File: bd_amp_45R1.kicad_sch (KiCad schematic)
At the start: 53 parts, among them Q2101 2SC3357, Q2102 2SC3357, T2101 XFMR_RF_BIFILAR, T2102 XFMR_RF_BIFILAR, U2101 AS169-73, U2102 AS169-73

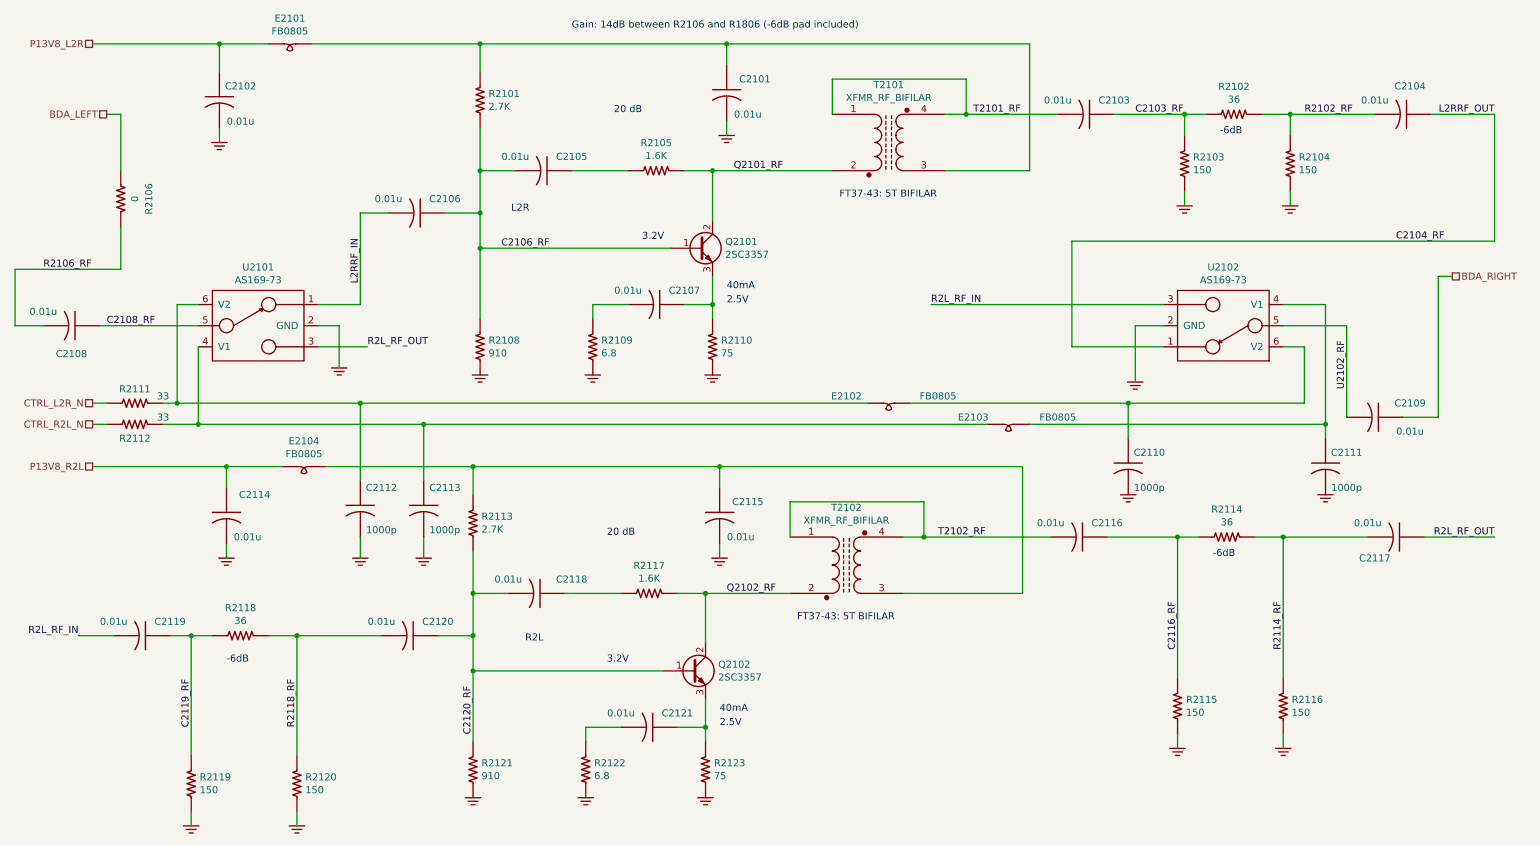
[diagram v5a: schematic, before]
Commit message: trx_mobo_concept_2_B. Change design to use a dedicated 8V supply for the 2SC3357 parts. Add S-Meter connector. Change mic connector to 3 pins and add 8V sopower supply to pin 3.
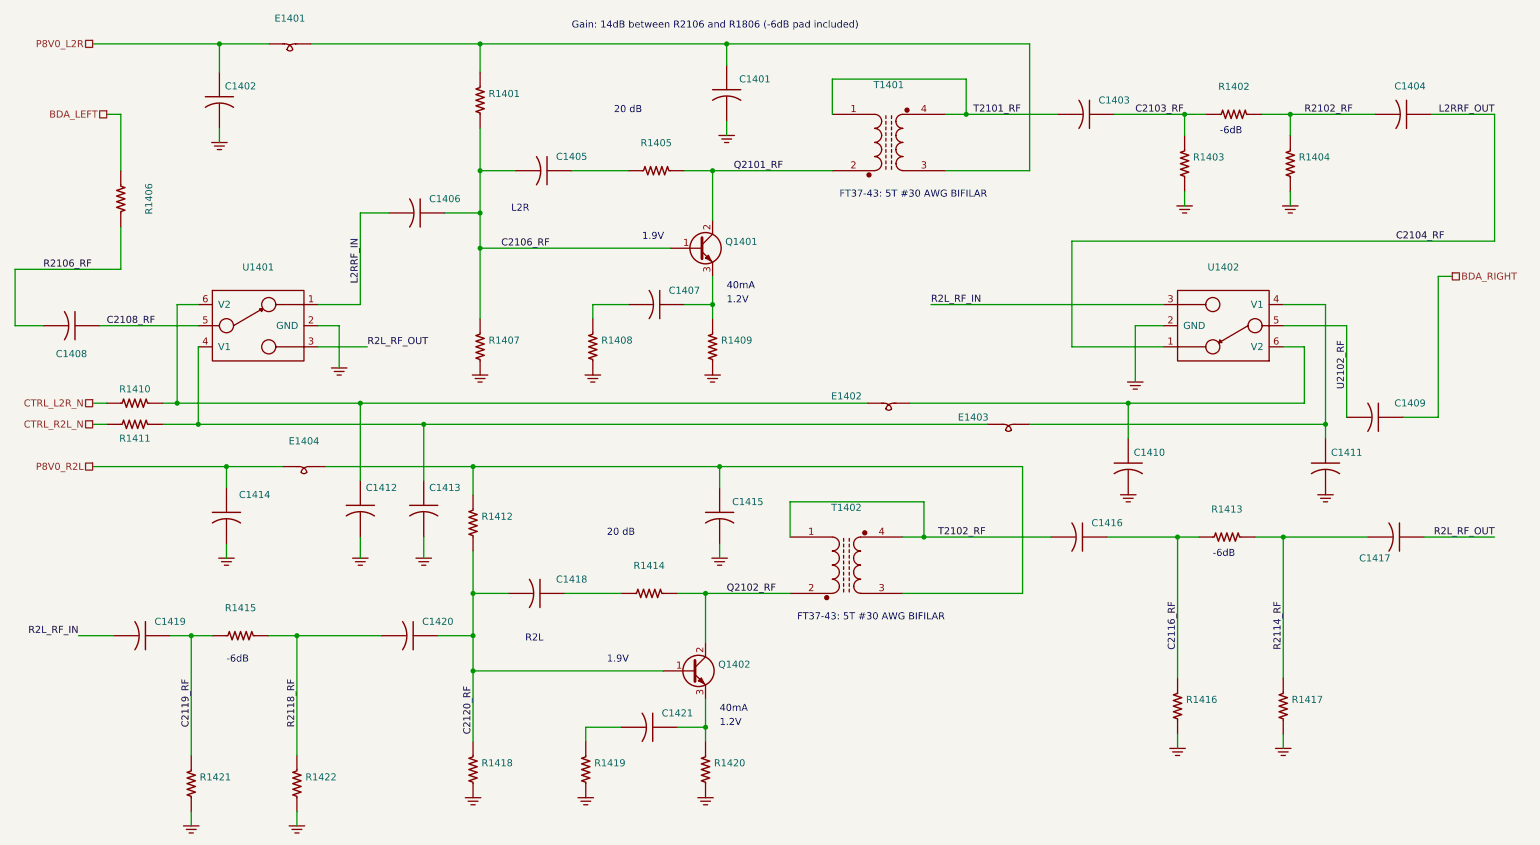
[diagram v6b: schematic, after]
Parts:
- C1401: renamed from C2101; value 0.01u -> (none); footprint Capacitor_SMD:C_0805_2012Metric_Pad1.18x1.45mm_HandSolder -> (none); PartNumber 800238-103 -> 800239-103
- C1402: renamed from C2102; value 0.01u -> (none); footprint Capacitor_SMD:C_0805_2012Metric_Pad1.18x1.45mm_HandSolder -> (none); PartNumber 800238-103 -> 800239-103
- C1403: renamed from C2103; value 0.01u -> (none); footprint Capacitor_SMD:C_0805_2012Metric_Pad1.18x1.45mm_HandSolder -> (none); PartNumber 800238-103 -> 800239-103
- C1404: renamed from C2104; value 0.01u -> (none); footprint Capacitor_SMD:C_0805_2012Metric_Pad1.18x1.45mm_HandSolder -> (none); PartNumber 800238-103 -> 800239-103
- C1405: renamed from C2105; value 0.01u -> (none); footprint Capacitor_SMD:C_0805_2012Metric_Pad1.18x1.45mm_HandSolder -> (none); PartNumber 800238-103 -> 800239-103
- C1406: renamed from C2106; value 0.01u -> (none); footprint Capacitor_SMD:C_0805_2012Metric_Pad1.18x1.45mm_HandSolder -> (none); PartNumber 800238-103 -> 800239-103
- C1407: renamed from C2107; value 0.01u -> (none); footprint Capacitor_SMD:C_0805_2012Metric_Pad1.18x1.45mm_HandSolder -> (none); PartNumber 800238-103 -> 800239-103
- C1408: renamed from C2108; value 0.01u -> (none); footprint Capacitor_SMD:C_0805_2012Metric_Pad1.18x1.45mm_HandSolder -> (none); PartNumber 800238-103 -> 800239-103
- C1409: renamed from C2109; value 0.01u -> (none); footprint Capacitor_SMD:C_0805_2012Metric_Pad1.18x1.45mm_HandSolder -> (none); PartNumber 800238-103 -> 800239-103
- C1410: renamed from C2110; value 1000p -> (none); footprint Capacitor_SMD:C_0805_2012Metric_Pad1.18x1.45mm_HandSolder -> (none)
- C1411: renamed from C2111; value 1000p -> (none); footprint Capacitor_SMD:C_0805_2012Metric_Pad1.18x1.45mm_HandSolder -> (none)
- C1412: renamed from C2112; value 1000p -> (none); footprint Capacitor_SMD:C_0805_2012Metric_Pad1.18x1.45mm_HandSolder -> (none)
- C1413: renamed from C2113; value 1000p -> (none); footprint Capacitor_SMD:C_0805_2012Metric_Pad1.18x1.45mm_HandSolder -> (none)
- C1414: renamed from C2114; value 0.01u -> (none); footprint Capacitor_SMD:C_0805_2012Metric_Pad1.18x1.45mm_HandSolder -> (none); PartNumber 800238-103 -> 800239-103
- C1415: renamed from C2115; value 0.01u -> (none); footprint Capacitor_SMD:C_0805_2012Metric_Pad1.18x1.45mm_HandSolder -> (none); PartNumber 800238-103 -> 800239-103
- C1416: renamed from C2116; value 0.01u -> (none); footprint Capacitor_SMD:C_0805_2012Metric_Pad1.18x1.45mm_HandSolder -> (none); PartNumber 800238-103 -> 800239-103
- C1417: renamed from C2117; value 0.01u -> (none); footprint Capacitor_SMD:C_0805_2012Metric_Pad1.18x1.45mm_HandSolder -> (none); PartNumber 800238-103 -> 800239-103
- C1418: renamed from C2118; value 0.01u -> (none); footprint Capacitor_SMD:C_0805_2012Metric_Pad1.18x1.45mm_HandSolder -> (none); PartNumber 800238-103 -> 800239-103
- C1419: renamed from C2119; value 0.01u -> (none); footprint Capacitor_SMD:C_0805_2012Metric_Pad1.18x1.45mm_HandSolder -> (none); PartNumber 800238-103 -> 800239-103
- C1420: renamed from C2120; value 0.01u -> (none); footprint Capacitor_SMD:C_0805_2012Metric_Pad1.18x1.45mm_HandSolder -> (none); PartNumber 800238-103 -> 800239-103
- C1421: renamed from C2121; value 0.01u -> (none); footprint Capacitor_SMD:C_0805_2012Metric_Pad1.18x1.45mm_HandSolder -> (none); PartNumber 800238-103 -> 800239-103
- E1401: renamed from E2101; value FB0805 -> (none); footprint Inductor_SMD:L_0805_2012Metric -> (none)
- E1402: renamed from E2102; value FB0805 -> (none); footprint Inductor_SMD:L_0805_2012Metric -> (none)
- E1403: renamed from E2103; value FB0805 -> (none); footprint Inductor_SMD:L_0805_2012Metric -> (none)
- E1404: renamed from E2104; value FB0805 -> (none); footprint Inductor_SMD:L_0805_2012Metric -> (none)
- Q1401: renamed from Q2101; value 2SC3357 -> (none); footprint Package_TO_SOT_SMD:SOT-89-3 -> (none)
- Q1402: renamed from Q2102; value 2SC3357 -> (none); footprint Package_TO_SOT_SMD:SOT-89-3 -> (none)
- R1401: renamed from R2101; value 2.7K -> (none); footprint Resistor_SMD:R_0805_2012Metric_Pad1.15x1.40mm_HandSolder -> (none); PartNumber 800235-272 -> 800235-112
- R1402: renamed from R2102; value 36 -> (none); footprint Resistor_SMD:R_0805_2012Metric_Pad1.15x1.40mm_HandSolder -> (none)
- R1403: renamed from R2103; value 150 -> (none); footprint Resistor_SMD:R_0805_2012Metric_Pad1.15x1.40mm_HandSolder -> (none)
- R1404: renamed from R2104; value 150 -> (none); footprint Resistor_SMD:R_0805_2012Metric_Pad1.15x1.40mm_HandSolder -> (none)
- R1405: renamed from R2105; value 1.6K -> (none); footprint Resistor_SMD:R_0805_2012Metric_Pad1.15x1.40mm_HandSolder -> (none)
- R1406: renamed from R2106; value 0 -> (none); footprint Resistor_SMD:R_0805_2012Metric_Pad1.15x1.40mm_HandSolder -> (none)
- R1407: renamed from R2108; value 910 -> (none); footprint Resistor_SMD:R_0805_2012Metric_Pad1.15x1.40mm_HandSolder -> (none); PartNumber 800235-911 -> 800235-361
- R1408: renamed from R2109; value 6.8 -> (none); footprint Resistor_SMD:R_0805_2012Metric_Pad1.15x1.40mm_HandSolder -> (none)
- R1409: renamed from R2110; value 75 -> (none); footprint Resistor_SMD:R_0805_2012Metric_Pad1.15x1.40mm_HandSolder -> (none); PartNumber 800235-750 -> 800235-300
- R1410: renamed from R2111; value 33 -> (none); footprint Resistor_SMD:R_0805_2012Metric_Pad1.15x1.40mm_HandSolder -> (none)
- R1411: renamed from R2112; value 33 -> (none); footprint Resistor_SMD:R_0805_2012Metric_Pad1.15x1.40mm_HandSolder -> (none)
- R1412: renamed from R2113; value 2.7K -> (none); footprint Resistor_SMD:R_0805_2012Metric_Pad1.15x1.40mm_HandSolder -> (none); PartNumber 800235-272 -> 800235-112
- R1413: renamed from R2114; value 36 -> (none); footprint Resistor_SMD:R_0805_2012Metric_Pad1.15x1.40mm_HandSolder -> (none)
- R1414: renamed from R2117; value 1.6K -> (none); footprint Resistor_SMD:R_0805_2012Metric_Pad1.15x1.40mm_HandSolder -> (none)
- R1415: renamed from R2118; value 36 -> (none); footprint Resistor_SMD:R_0805_2012Metric_Pad1.15x1.40mm_HandSolder -> (none)
- R1416: renamed from R2115; value 150 -> (none); footprint Resistor_SMD:R_0805_2012Metric_Pad1.15x1.40mm_HandSolder -> (none)
- R1417: renamed from R2116; value 150 -> (none); footprint Resistor_SMD:R_0805_2012Metric_Pad1.15x1.40mm_HandSolder -> (none)
- R1418: renamed from R2121; value 910 -> (none); footprint Resistor_SMD:R_0805_2012Metric_Pad1.15x1.40mm_HandSolder -> (none); PartNumber 800235-911 -> 800235-361
- R1419: renamed from R2122; value 6.8 -> (none); footprint Resistor_SMD:R_0805_2012Metric_Pad1.15x1.40mm_HandSolder -> (none)
- R1420: renamed from R2123; value 75 -> (none); footprint Resistor_SMD:R_0805_2012Metric_Pad1.15x1.40mm_HandSolder -> (none); PartNumber 800235-750 -> 800235-300
- R1421: renamed from R2119; value 150 -> (none); footprint Resistor_SMD:R_0805_2012Metric_Pad1.15x1.40mm_HandSolder -> (none)
- R1422: renamed from R2120; value 150 -> (none); footprint Resistor_SMD:R_0805_2012Metric_Pad1.15x1.40mm_HandSolder -> (none)
- T1401: renamed from T2101; value XFMR_RF_BIFILAR -> (none); footprint mods:XFMR_Handwound_FT37 -> (none)
- T1402: renamed from T2102; value XFMR_RF_BIFILAR -> (none); footprint mods:XFMR_Handwound_FT37 -> (none)
- U1401: renamed from U2101; value AS169-73 -> (none); footprint Package_TO_SOT_SMD:SOT-23-6 -> (none)
- U1402: renamed from U2102; value AS169-73 -> (none); footprint Package_TO_SOT_SMD:SOT-23-6 -> (none)
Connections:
- net P13V8_L2R renamed P8V0_L2R
- net P13V8_R2L renamed P8V0_R2L
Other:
- note added: "1.2V"
- note added: "1.9V"
- note added: "FT37-43: 5T #30 AWG BIFILAR"
- note removed: "2.5V"
- note removed: "3.2V"
- note removed: "FT37-43: 5T BIFILAR"
